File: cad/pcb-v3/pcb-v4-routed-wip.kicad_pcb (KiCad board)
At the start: 4 copper layers, 19.3 x 19.3 mm, 50 parts

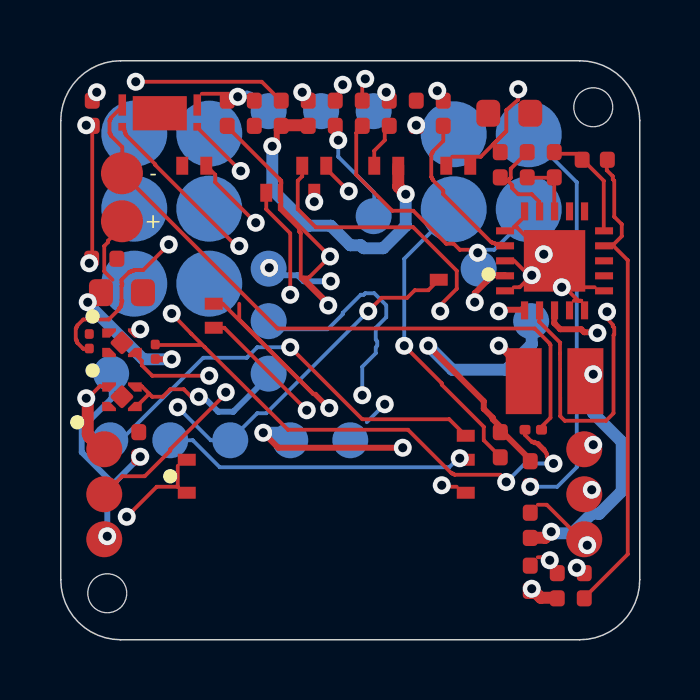
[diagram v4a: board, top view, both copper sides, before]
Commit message: Via floor -> JLC standard 0.45/0.20; blockers 7 -> 3, DRC clean
fab_floor_touchid.txt's 0.60/0.30 was the only entry in that file with no
comment justifying it -- the tell that it was a carried-over KiCad default
rather than a decision. py_router/fab_tiers.py (citing JLC 2026-06) puts the
standard, NO-EXTRA-COST tier at via 0.45 dia / 0.20 drill, and preflight
check 8 independently uses the same pair. The aspect-ratio objection does not
apply either: 1.20 mm board / 0.20 mm drill = 6:1, against the 8:1+ fabs run
routinely. Reasoning is now written into the file so it is not re-litigated.

Three scripts had their own hard-coded copies of rules that live in that file,
and all three drifted:
  * gnd_taps.py  had VIA_D/VIA_DRILL hard-coded -- emitted taps at one size
    while check_drc graded at another. 23 phantom violations came from this.
  * handroute.py had TRACK/CLR frozen at 0.20/0.20 after the board moved to
    0.127/0.10, so every 'no path' it reported was measured with a track 57%
    too wide. stitch_open's docstring flagged this months ago; the fix was
    made in a scratch copy and never committed, so it kept lying.
  * stitch_open.py under-covered custom pads (fixed in the previous commit).
All three now read fab_floor_touchid.txt. One source of truth.

Routing: SENSOR_SW_EN joins the stage-1 pre-route list (it kept coming out
empty when routed late). 29/30 nets carry copper, only GND empty as intended.

  open pads   16 -> 8        taps  15 -> 24        DRC  46 -> 0
  blockers: 2, 6, 6b, 17, 18, 20, 21  ->  6, 17, 18

Remaining 3 stitch failures (CELL_NEG C14.2, RESET R7.2, SENSOR_3V3 C6.1)
resist handroute at correct rules. 17 and 18 are both the KiCad zone fill.
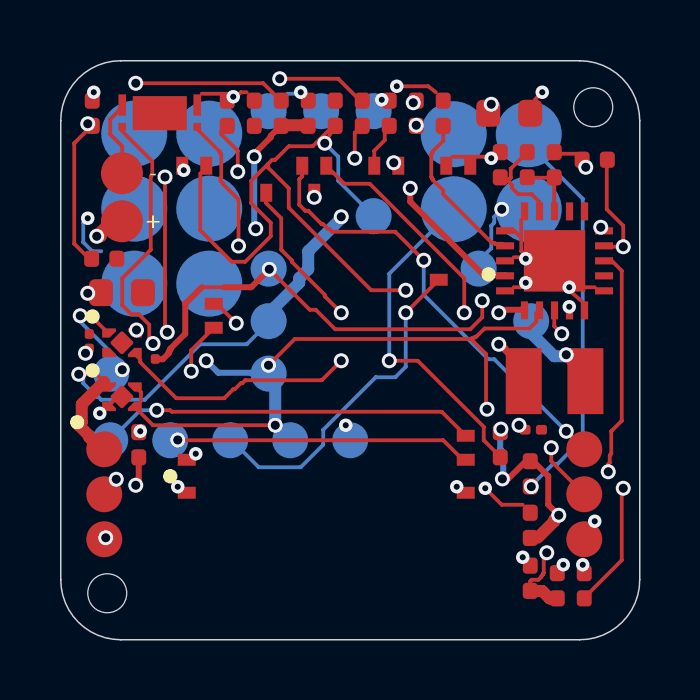
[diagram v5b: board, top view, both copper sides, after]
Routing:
- net VBAT_OK: track 10.1 -> 42.4 mm, vias 2 -> 3
- net BL_FLAG: track 37.2 -> 16.5 mm, vias 4 -> 3
- net CELL_NEG: track 22.2 -> 2.66 mm
- net VSTOR: track 67.1 -> 50.0 mm, vias 8 -> 9
- net RESET: track 26.1 -> 11.3 mm, vias 3 -> 1
- net VIN_DC: track 29.1 -> 37.7 mm, vias 4 -> 6
- net SENSOR_3V3: track 23.0 -> 28.9 mm, vias 2 -> 3
- net GND: track 17.4 -> 11.8 mm, vias 15 -> 24
- net VBAT: track 26.4 -> 31.2 mm
- net VBAT_SENSE: track 28.6 -> 23.9 mm, vias 4 -> 5
- net SENSOR_MCU_3V3: track 7.88 -> 12.5 mm, vias 2 -> 4
- net SENSOR_SW_EN: track 10.5 -> 14.8 mm
- net SENSOR_RX: track 18.7 -> 15.0 mm
- net PCM_VDD: track 27.4 -> 31.0 mm, vias 4 -> 2
- net SWDIO: track 14.4 -> 12.6 mm
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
